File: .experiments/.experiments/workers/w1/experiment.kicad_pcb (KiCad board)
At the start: 2 copper layers, 140 x 90 mm, 39 parts, among them J1 USB_C, J2 Output, J3 Debug, Q1 FS8205A, U1 USBLC6-2SC6, U2 BQ24072, U3 HY2113-KB5B, U4 MT3608, U5 AP2112K-3.3, U6 LN61CN3302MR-G

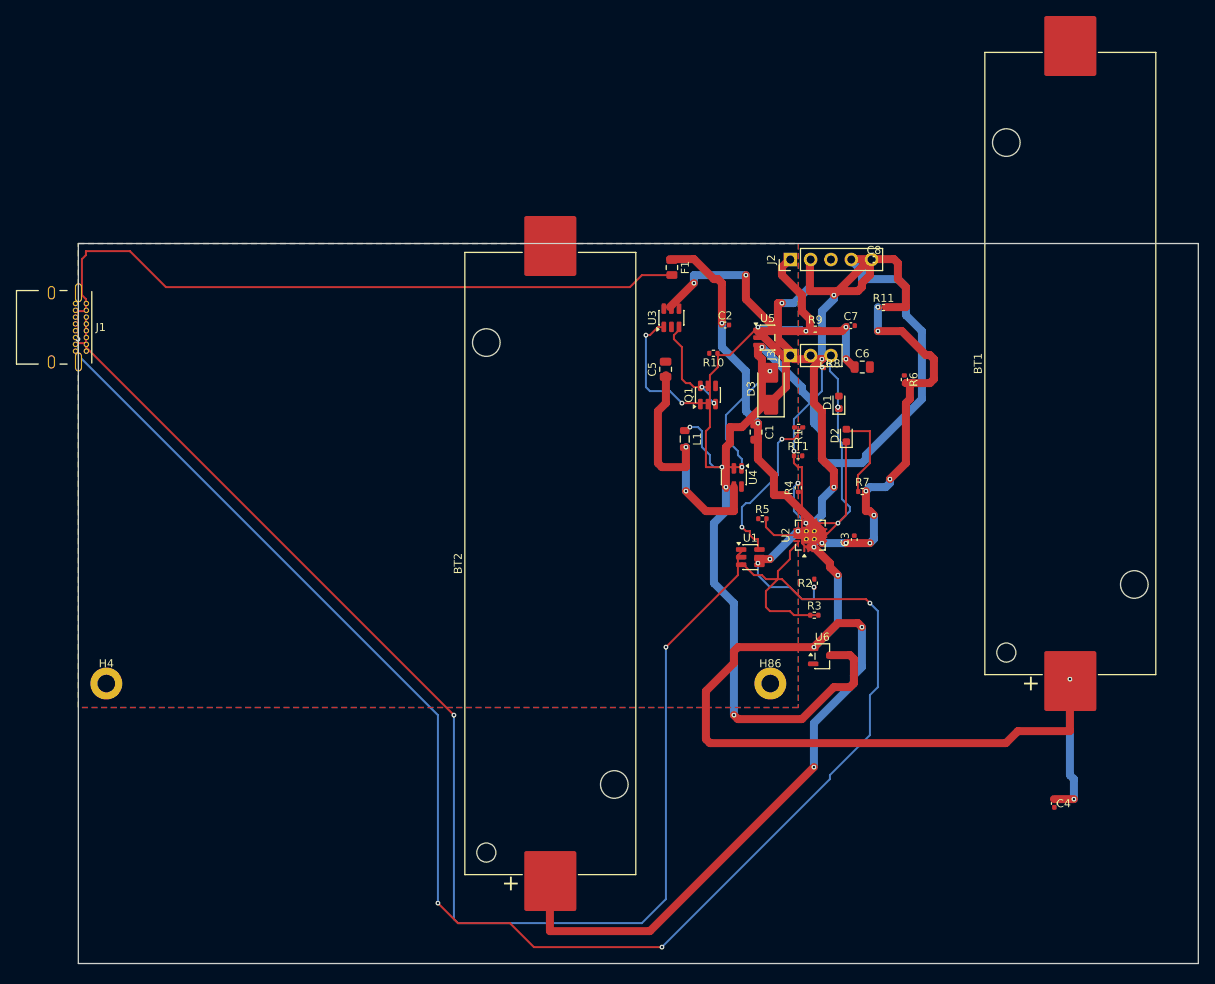
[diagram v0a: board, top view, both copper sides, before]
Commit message: Set uniform 6mil trace width (0.1524mm) for signal+power to reduce shorts
Baseline with 6mil: score=20.05 shorts=72 (vs 25.66@82shorts before)
Round 1: 20.45 shorts=93
Round 2: 20.65 shorts=84 [NEW BEST]
Round 3: 19.44 shorts=72

Trading off routing flexibility for cleaner DRC (no catastrophic shorts).
Tighter routing but more predictable.

Co-Authored-By: Claude Opus 4.6 <noreply@anthropic.com>
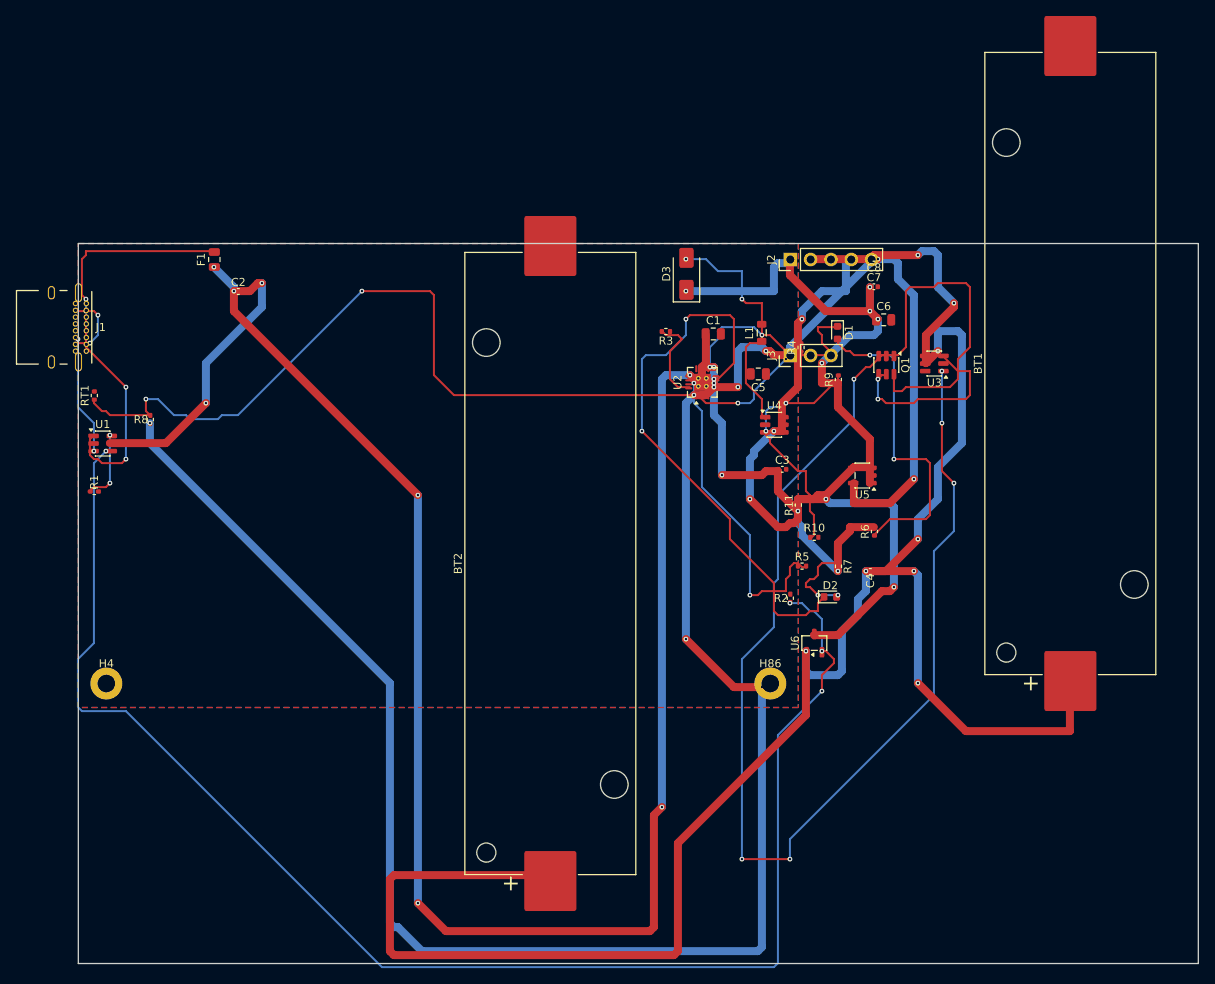
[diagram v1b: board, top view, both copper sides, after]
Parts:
- moved R1 88.4 mm to (2.00, 31.0), turned to 0 degrees
- moved RT1 88.3 mm to (2.00, 19.0), turned to 90 degrees
- moved R8 84.5 mm to (9.00, 22.0), turned to 90 degrees
- moved U1 82.2 mm to (3.04, 25.0)
- moved C2 61.0 mm to (20.0, 6.00)
- moved F1 57.2 mm to (17.0, 2.00), turned to 90 degrees
- moved R3 40.0 mm to (73.4, 11.0), turned to 180 degrees
- moved C4 37.0 mm to (99.0, 41.0), turned to 180 degrees
- moved U3 33.4 mm to (107.0, 15.0), turned to 180 degrees
- moved R11 26.9 mm to (90.0, 32.7), turned to 90 degrees
- moved R10 26.2 mm to (92.0, 36.7), turned to 0 degrees
- moved U2 23.4 mm to (78.0, 17.4)
- moved Q1 22.6 mm to (101.0, 15.2), turned to -90 degrees
- moved U5 20.9 mm to (98.0, 29.0), turned to 180 degrees
- moved D2 20.3 mm to (94.0, 44.2), turned to 0 degrees
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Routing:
- net /VBAT: track 253.3 -> 479.1 mm, vias 12 -> 16
- net /VBUS: track 52.8 -> 236.8 mm, vias 4 -> 8
- net Net-(J1-CC2): track 192.1 -> 14.8 mm, vias 4 -> 2
- net Net-(R2-Pad1): track 11.2 -> 186.8 mm, vias 2 -> 4
- net Net-(J1-CC1): track 169.9 -> 27.9 mm
- net Net-(Q1A-G): track 17.7 -> 147.2 mm, vias 2 -> 6
- net /NTC_SENSE: track 27.0 -> 115.7 mm, vias 2 -> 4
- net Net-(D2-K): track 13.0 -> 70.6 mm, vias 0 -> 2
- net Net-(F1-Pad2): track 89.4 -> 32.0 mm, vias 0 -> 4
- net /EN: track 146.3 -> 93.4 mm, vias 4 -> 6
- net Net-(D1-A): track 0.00 -> 40.1 mm, vias 0 -> 2
- net Net-(Q1A-D): track 2.62 -> 42.3 mm, vias 2 -> 0
- net Net-(U2-TMR): track 5.41 -> 40.4 mm, vias 0 -> 2
- net /VSYS_BOOST: track 33.2 -> 0.00 mm, vias 2 -> 0
- net /5V: track 38.8 -> 66.5 mm, vias 2 -> 6
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
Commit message: Clean up: remove 50M+ of old experiment artifacts
Removed:
- .tmp_router_regression/ (11M baseline)
- .experiments/workers/ (40M+ old copies)
- .experiments/frames/ (old snapshots)

Kept: latest PCB, GIF, config, results

Co-Authored-By: Claude Opus 4.6 <noreply@anthropic.com>
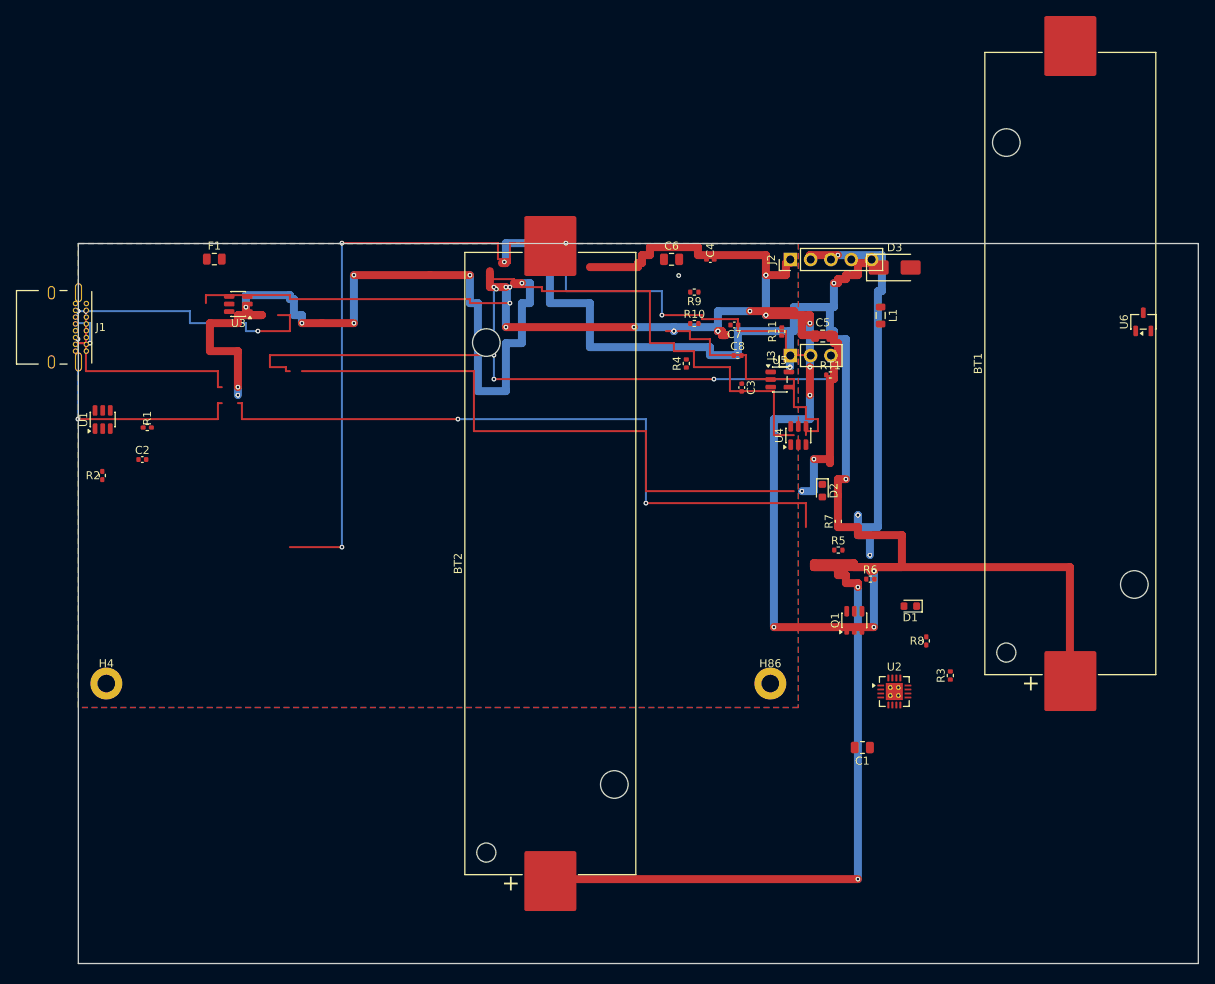
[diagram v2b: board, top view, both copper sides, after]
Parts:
- moved R8 100.9 mm to (106.0, 49.7)
- moved RT1 92.0 mm to (94.0, 16.4), turned to 0 degrees
- moved R2 87.4 mm to (3.00, 29.0)
- moved U3 87.3 mm to (20.0, 7.56)
- moved U6 57.5 mm to (133.1, 9.79)
- moved R3 55.8 mm to (109.0, 54.0), turned to 90 degrees
- moved C1 55.0 mm to (98.0, 63.0), turned to 180 degrees
- moved U2 45.5 mm to (102.0, 56.0), turned to 0 degrees
- moved C4 43.8 mm to (79.0, 2.00), turned to 0 degrees
- moved D1 35.4 mm to (104.0, 45.3), turned to 180 degrees
- moved Q1 32.2 mm to (97.0, 47.1), turned to 90 degrees
- moved R10 30.6 mm to (77.0, 10.0)
- moved C6 27.6 mm to (74.2, 1.97)
- moved D3 26.0 mm to (102.0, 3.00), turned to 0 degrees
- moved C2 24.2 mm to (8.00, 27.0)
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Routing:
- net /VBAT: track 479.1 -> 279.5 mm, vias 16 -> 10
- net Net-(Q1A-G): track 147.2 -> 0.00 mm, vias 6 -> 0
- net /VBUS: track 236.8 -> 99.5 mm
- net Net-(R2-Pad1): track 186.8 -> 86.5 mm, vias 4 -> 2
- net /EN: track 93.4 -> 0.00 mm, vias 6 -> 0
- net /CHG_N: track 27.2 -> 99.5 mm, vias 3 -> 6
- net /5V: track 66.5 -> 112.0 mm, vias 6 -> 11
- net Net-(Q1A-D): track 42.3 -> 0.00 mm
- net Net-(U2-ILIM): track 0.00 -> 42.0 mm, vias 0 -> 2
- net Net-(U2-TMR): track 40.4 -> 0.00 mm, vias 2 -> 0
- net /VSYS: track 47.3 -> 85.5 mm, vias 6 -> 10
- net Net-(D1-A): track 40.1 -> 76.5 mm, vias 2 -> 0
- net Net-(D3-A): track 31.1 -> 0.00 mm, vias 2 -> 0
- net Net-(U4-FB): track 30.4 -> 0.00 mm, vias 2 -> 0
- net Net-(Q1B-G): track 23.2 -> 0.00 mm, vias 2 -> 0
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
